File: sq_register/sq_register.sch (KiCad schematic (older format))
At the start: 0 parts

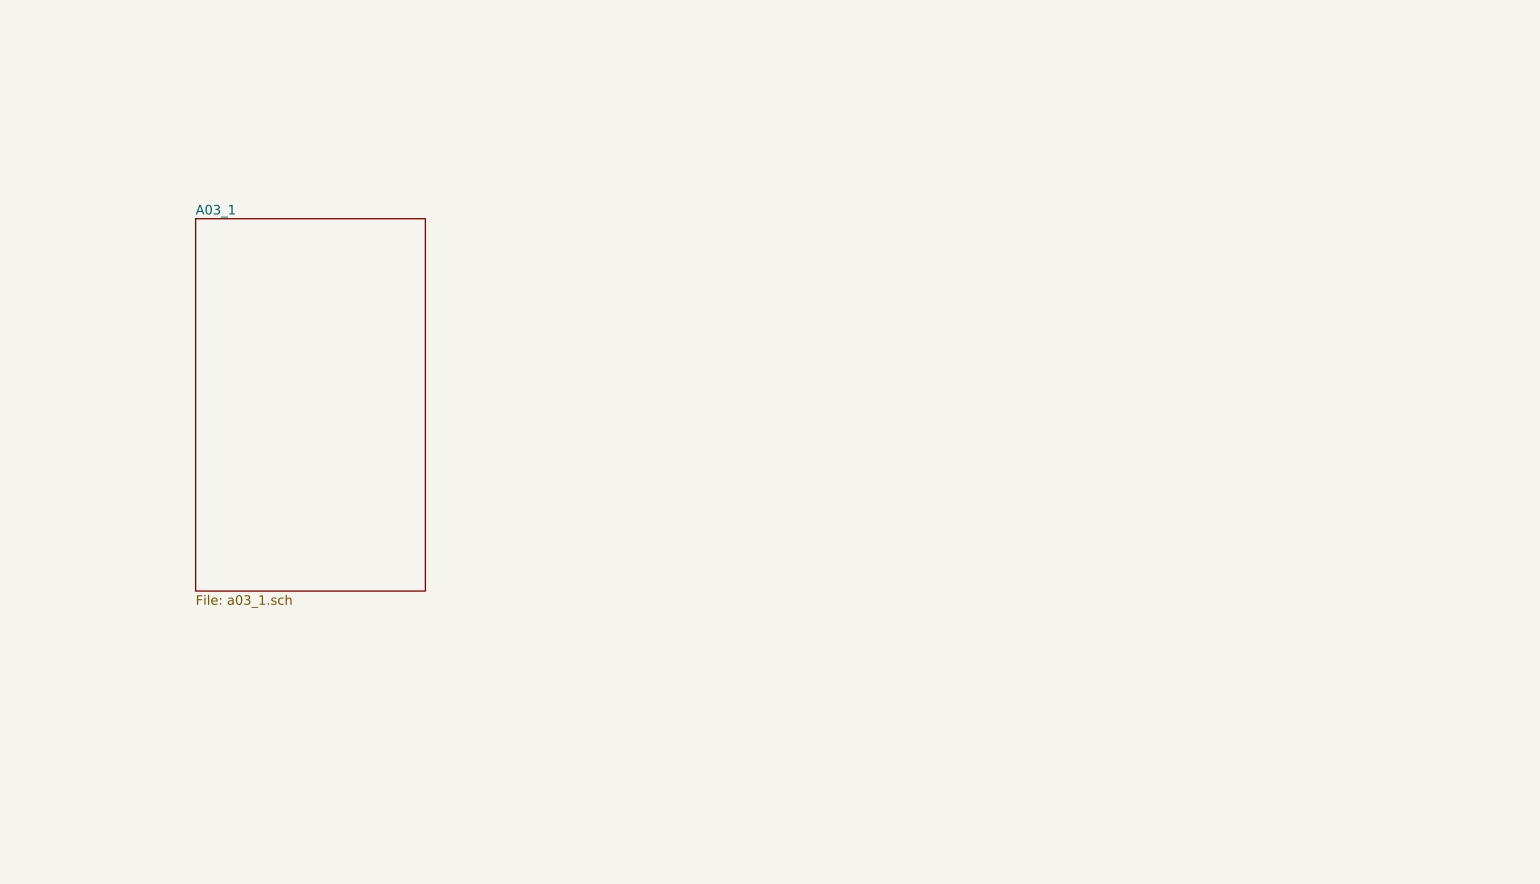
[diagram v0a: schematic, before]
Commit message: Filled out the rest of page A03-1. At the very least, it appears to be properly handling the GOJAM condition. Haven't looked much at non-GOJAM behavior. I also exposed T01..T12 and T01/..T12/ as outputs of the timer module. I'm going to need a bigger (or another) connector there soon
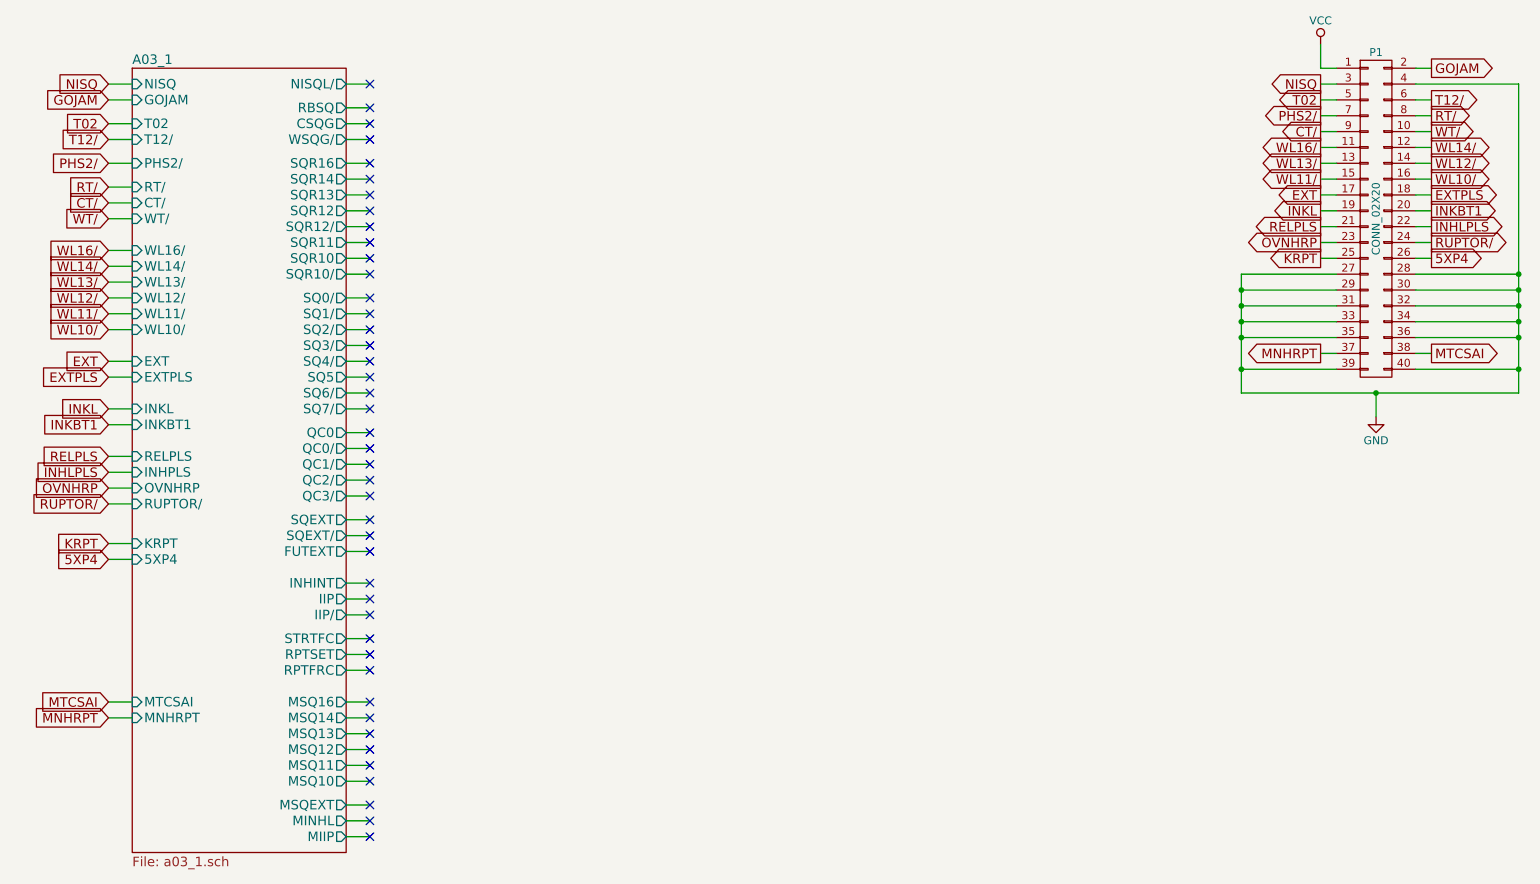
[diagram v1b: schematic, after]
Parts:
- added P1: CONN_02X20, symbol CONN_02X20
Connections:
- new net 5XP4: P1.26 (P26)
- new net CT/: P1.9 (P9)
- new net EXT: P1.17 (P17)
- new net EXTPLS: P1.18 (P18)
- new net GND: P1.27 (P27), P1.28 (P28), P1.29 (P29), P1.30 (P30), P1.31 (P31), P1.32 (P32), P1.33 (P33), P1.34 (P34), P1.35 (P35), P1.36 (P36), P1.39 (P39), P1.4 (P4), P1.40 (P40)
- new net GOJAM: P1.2 (P2)
- new net INHLPLS: P1.22 (P22)
- new net INKBT1: P1.20 (P20)
- new net INKL: P1.19 (P19)
- new net KRPT: P1.25 (P25)
- new net MNHRPT: P1.37 (P37)
- new net MTCSAI: P1.38 (P38)
- new net NISQ: P1.3 (P3)
- new net OVNHRP: P1.23 (P23)
- new net PHS2/: P1.7 (P7)
- new net RELPLS: P1.21 (P21)
- new net RT/: P1.8 (P8)
- new net RUPTOR/: P1.24 (P24)
- new net T02: P1.5 (P5)
- new net T12/: P1.6 (P6)
- new net VCC: P1.1 (P1)
- new net WL10/: P1.16 (P16)
- new net WL11/: P1.15 (P15)
- new net WL12/: P1.14 (P14)
- new net WL13/: P1.13 (P13)
- new net WL14/: P1.12 (P12)
- new net WL16/: P1.11 (P11)
- new net WT/: P1.10 (P10)
- no-connect marks 0 -> 43

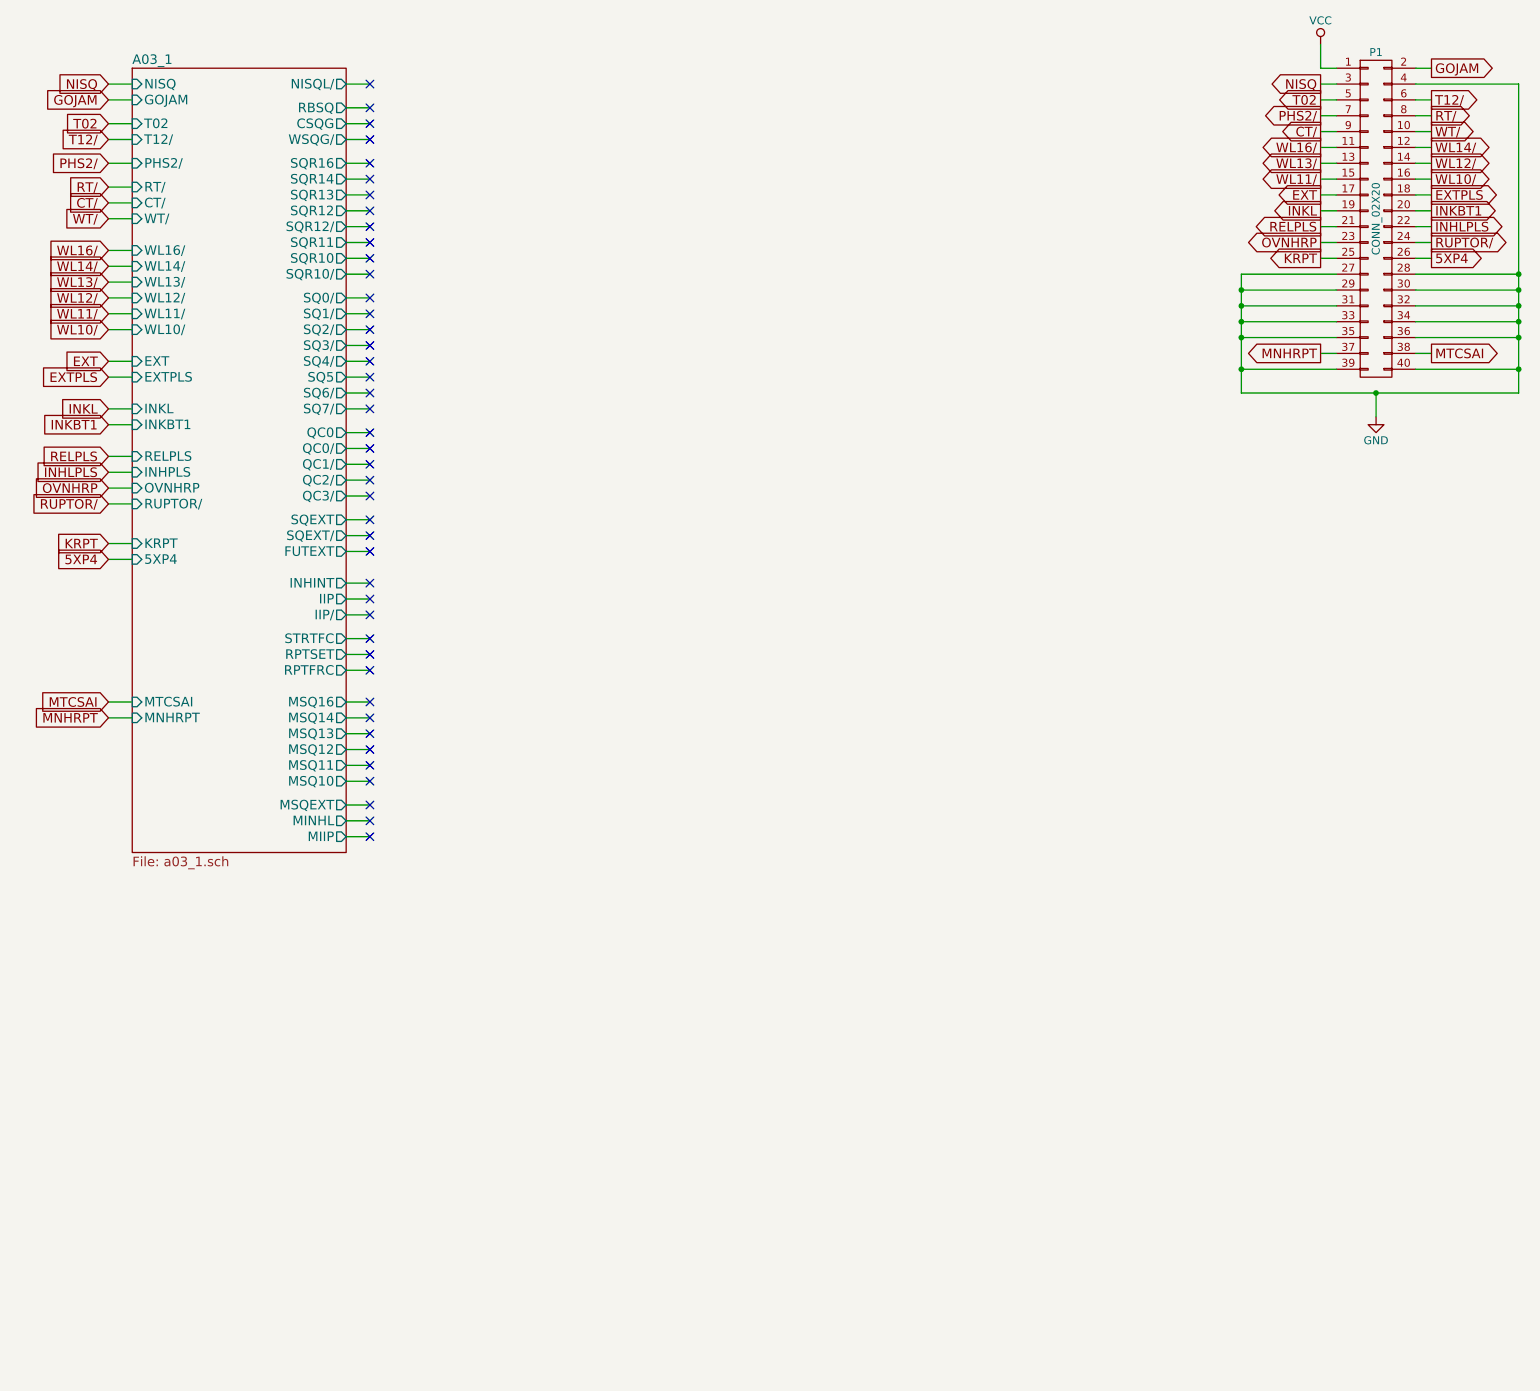
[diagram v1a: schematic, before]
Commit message: Finished off the SQ Register and Decoder module. Next up is the stage and branch registers
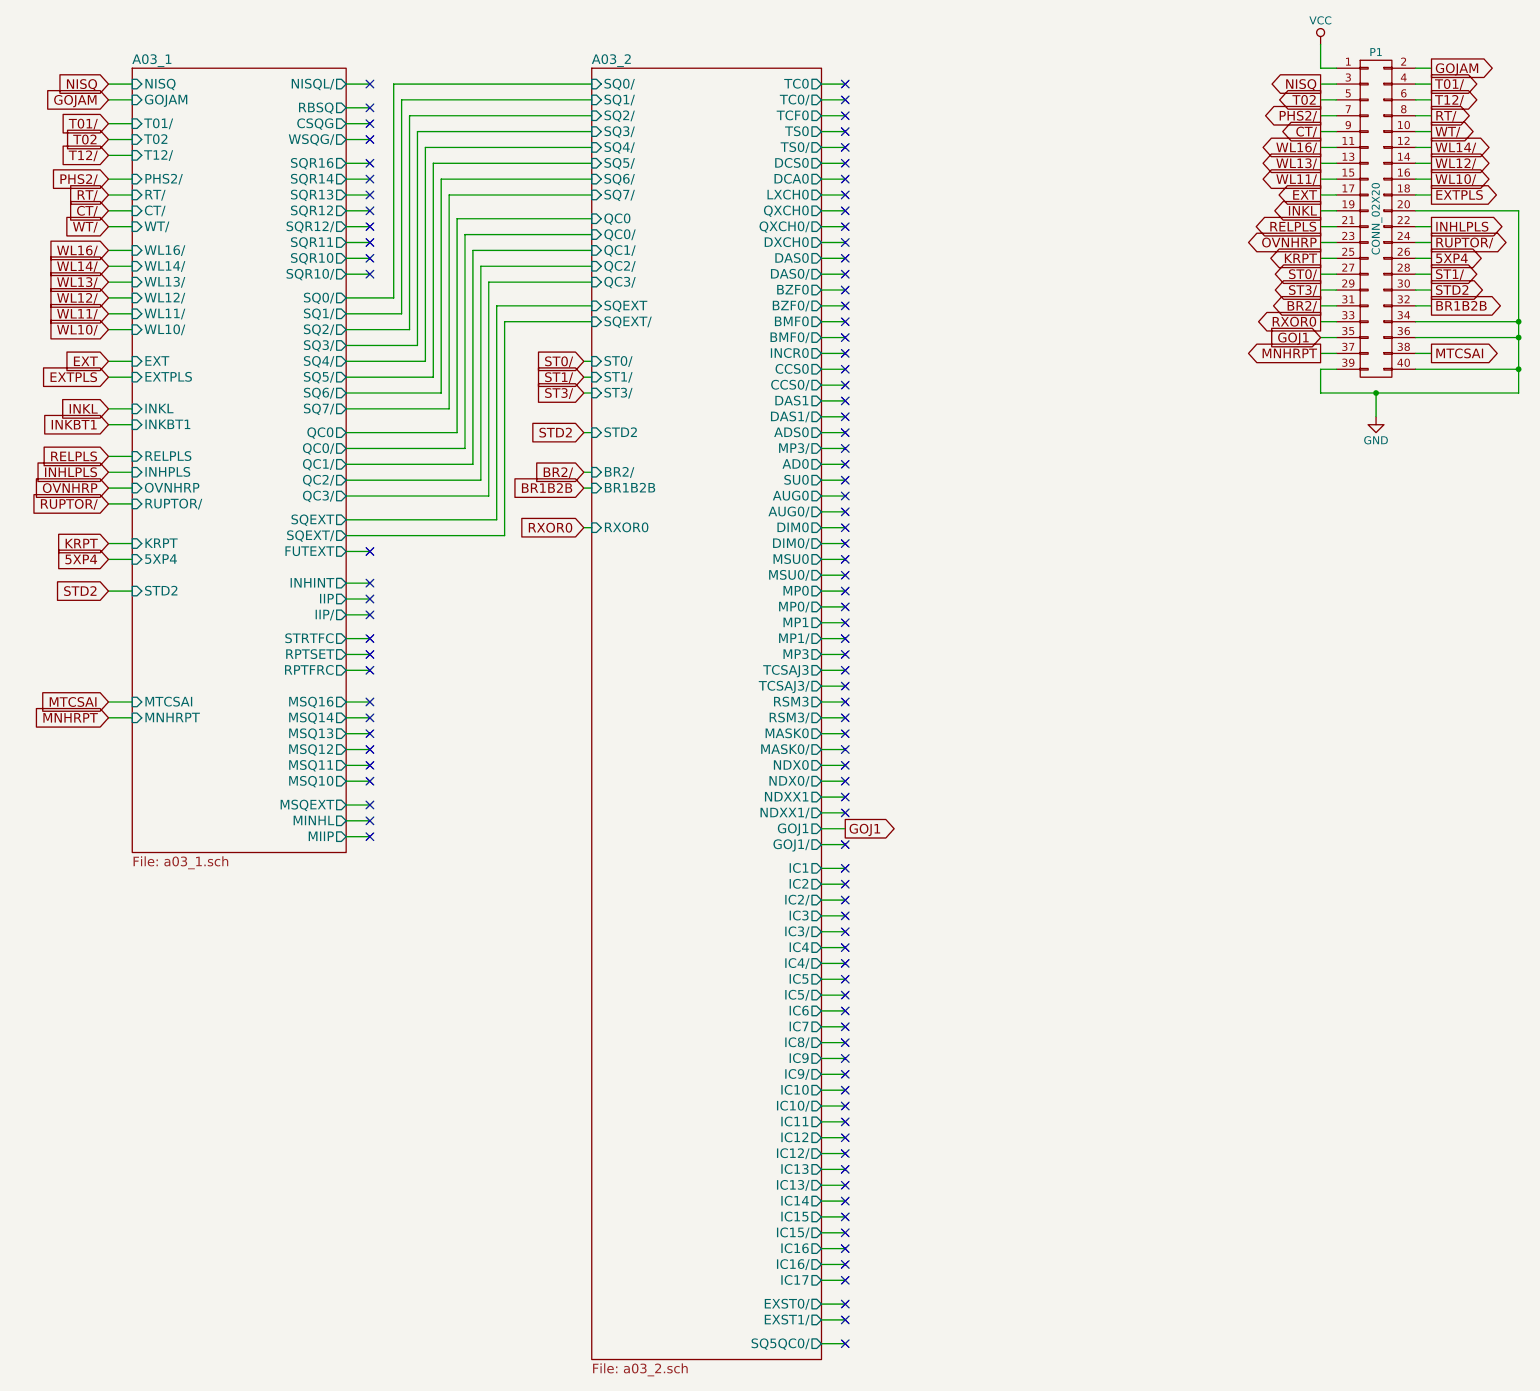
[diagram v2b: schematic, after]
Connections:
- net GND: now also P1.20 (P20); no longer P1.27 (P27), P1.28 (P28), P1.29 (P29), P1.30 (P30), P1.31 (P31), P1.32 (P32), P1.33 (P33), P1.35 (P35), P1.4 (P4)
- net INKBT1: no longer P1.20 (P20)
- new net BR1B2B: P1.32 (P32)
- new net BR2/: P1.31 (P31)
- new net GOJ1: P1.35 (P35)
- new net RXOR0: P1.33 (P33)
- new net ST0/: P1.27 (P27)
- new net ST1/: P1.28 (P28)
- new net ST3/: P1.29 (P29)
- new net STD2: P1.30 (P30)
- new net T01/: P1.4 (P4)
- no-connect marks 43 -> 106

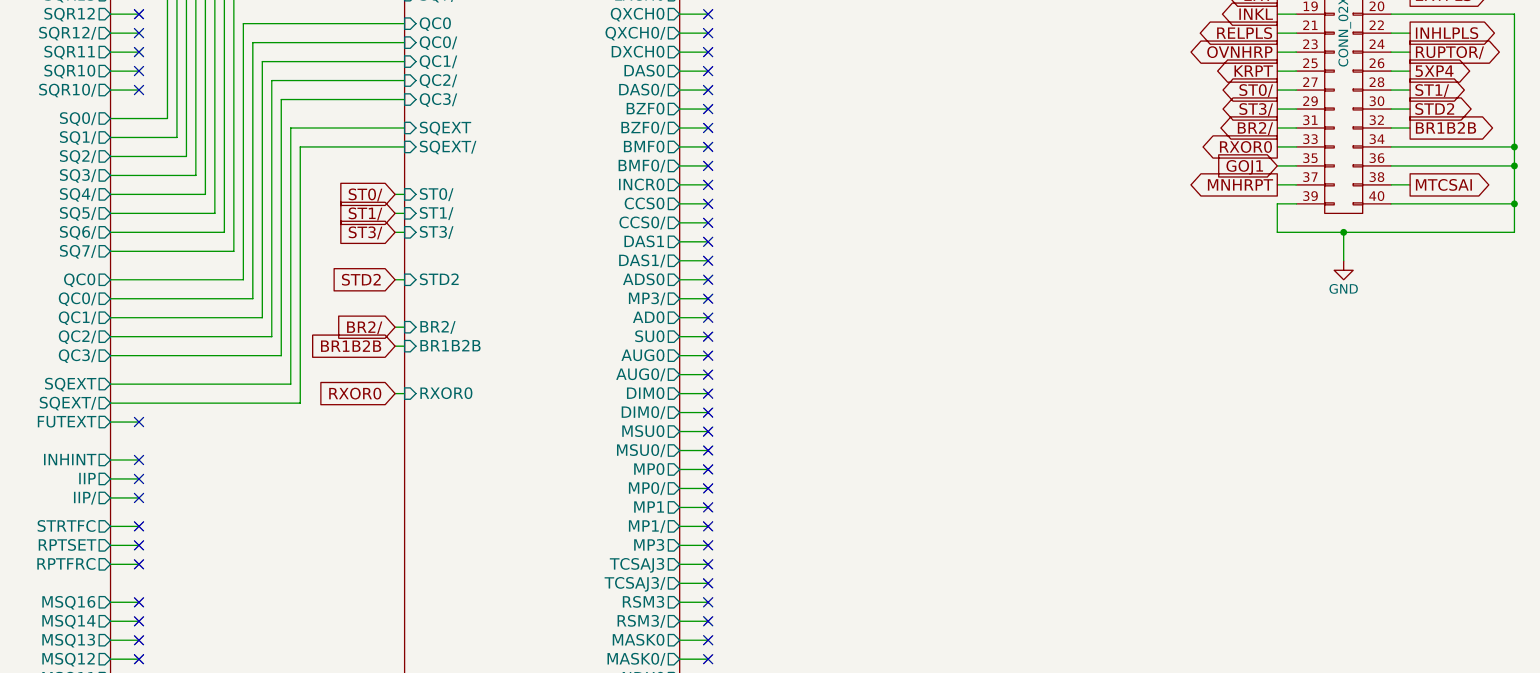
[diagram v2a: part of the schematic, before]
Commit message: Added the 'stage' bit of the Stage Branch Decoder module, and cleaned up a lot of initial conditions (still probably a lot to be done there)
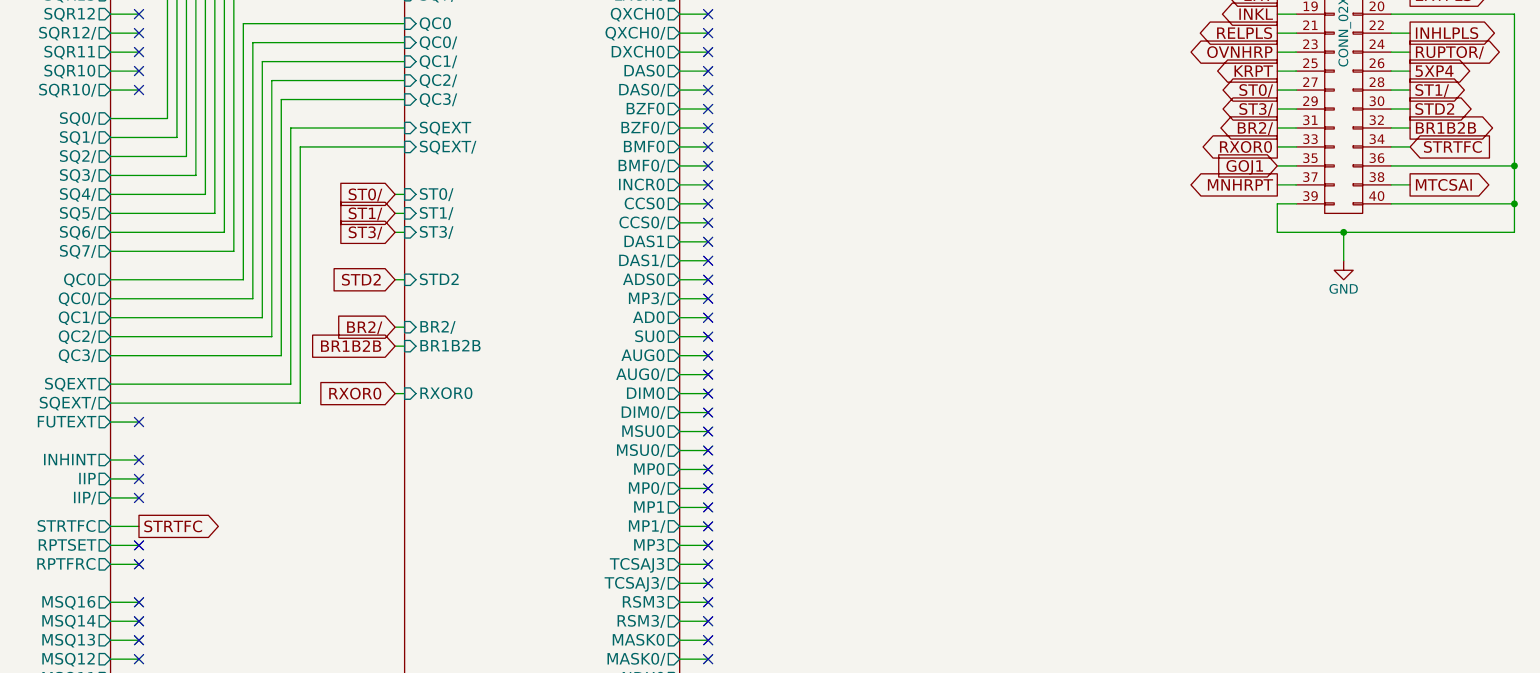
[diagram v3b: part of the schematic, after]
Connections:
- net GND: no longer P1.34 (P34)
- new net STRTFC: P1.34 (P34)
- no-connect marks 106 -> 105
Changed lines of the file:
@@
 NoConn ~ 3350 4300
 NoConn ~ 3350 4400
-NoConn ~ 3350 4550
 NoConn ~ 3350 4650
 NoConn ~ 3350 4750
@@
 	9950 2750 10050 2750
 Wire Wire Line
-	9950 2550 10600 2550
-Wire Wire Line
 	9950 2650 10600 2650
 Connection ~ 10600 2650
@@
 Wire Wire Line
 	10600 1850 10600 3000
-Connection ~ 10600 2550
+Text GLabel 3350 4550 2    60   Output ~ 0
+STRTFC
+Text GLabel 10050 2550 2    60   Input ~ 0
+STRTFC
+Wire Wire Line
+	10050 2550 9950 2550
 $EndSCHEMATC
